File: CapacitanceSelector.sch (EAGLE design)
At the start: 12 parts

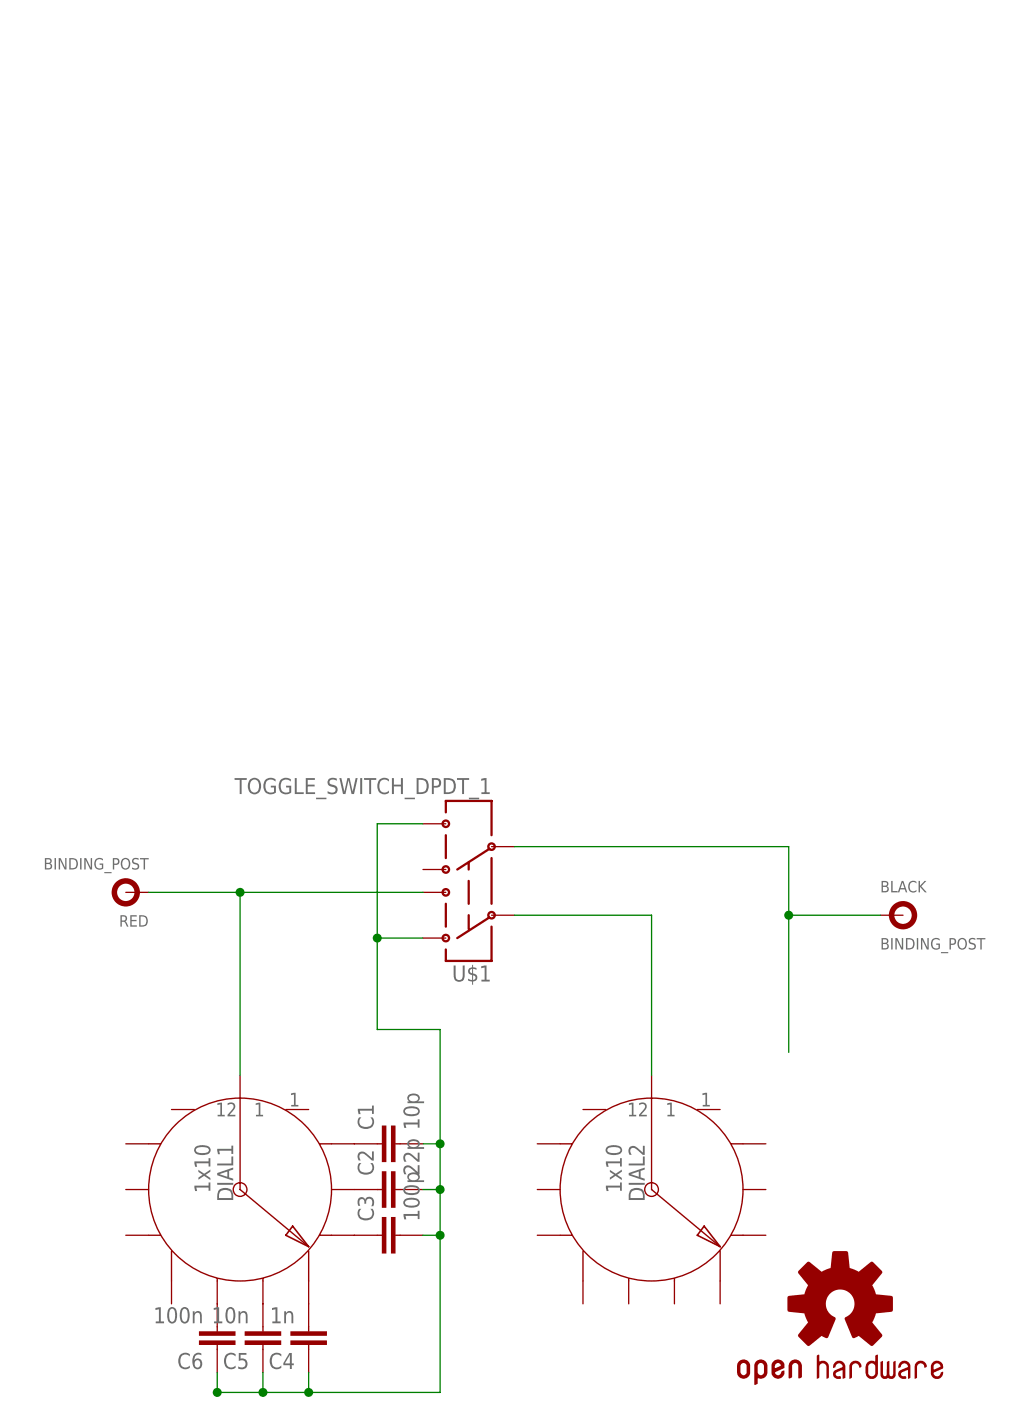
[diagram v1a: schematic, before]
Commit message: This is going to be an overly expensive board
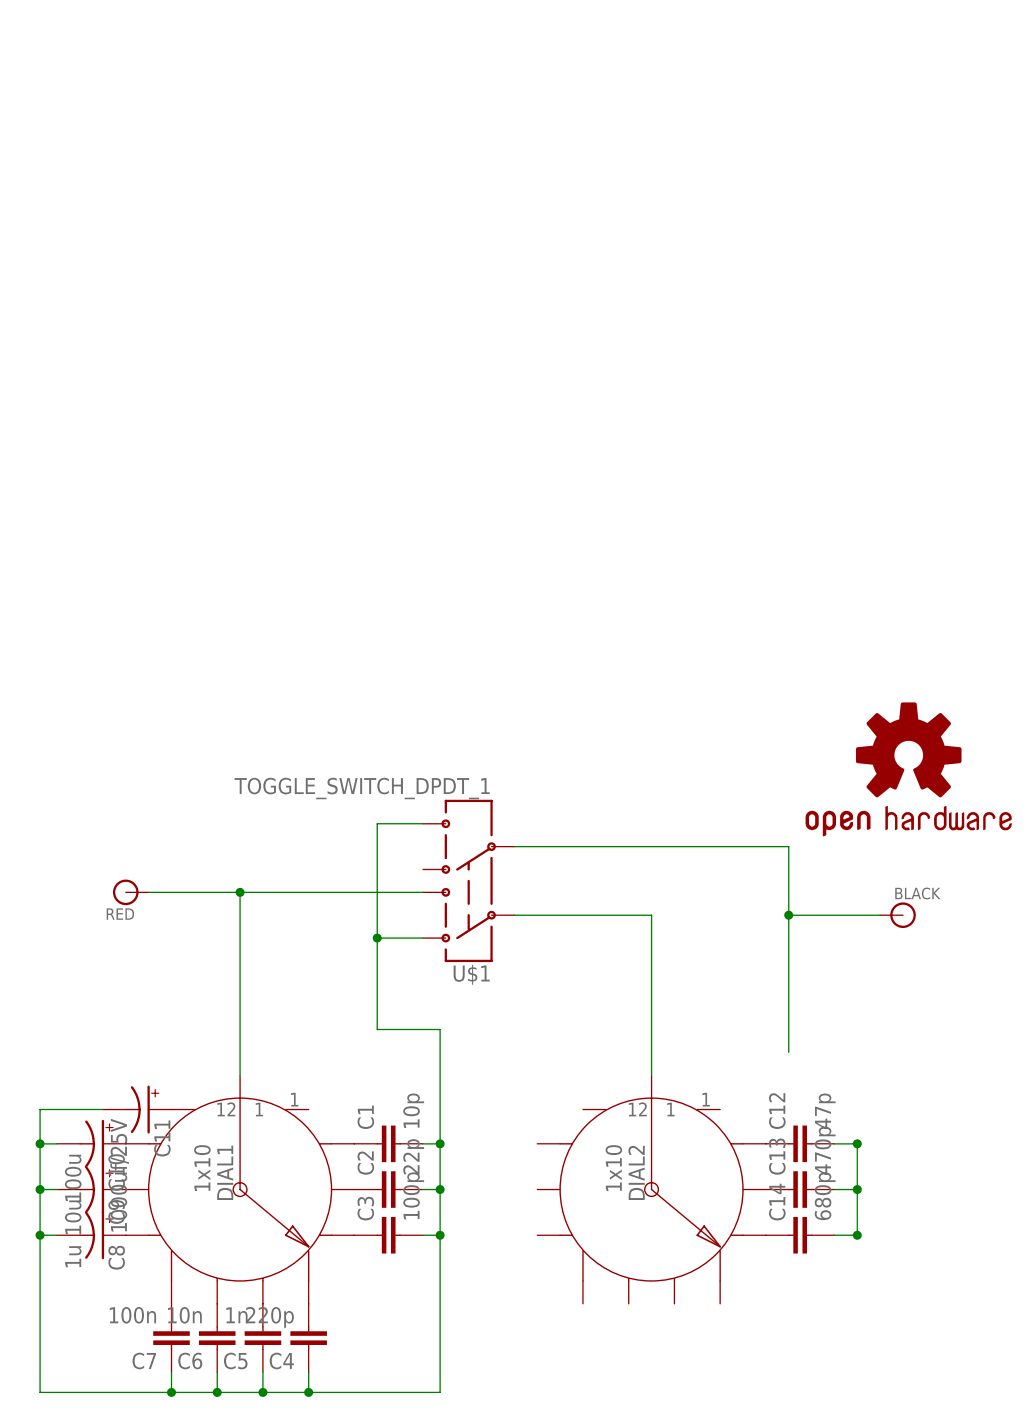
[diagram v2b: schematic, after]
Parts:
- added C10: 100u, SparkFun-Capacitors:10UF-25V-20%(PTH)KIT
- added C11: 1000uf/25V, SparkFun-Capacitors:1000UF-25V(PTH)KIT
- added C12: 47p, SparkFun-Capacitors:CAP_
- added C13: 470p, SparkFun-Capacitors:0.1UF-50V-20%(PTH)KIT-EZ
- added C14: 680p, SparkFun-Capacitors:0.1UF-50V-20%(PTH)KIT-EZ
- added C7: 100n, SparkFun-Capacitors:0.1UF-50V-20%(PTH)KIT-EZ
- added C8: 1u, SparkFun-Capacitors:10UF-25V-20%(PTH)KIT
- added C9: 10u, SparkFun-Capacitors:10UF-25V-20%(PTH)KIT
- BLACK, RED: value BINDING_POST -> (none); device SparkFun-Connectors:BINDING_POST -> SparkFun-Connectors:BANANA_CONN
- C4: value 1n -> 220p
- C5: value 10n -> 1n
- C6: value 100n -> 10n
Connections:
- new net N$11: C13.1, DIAL2.3
- new net N$13: C8.+, DIAL1.9
- new net N$14: C12.2, C13.2, C14.2
- new net N$15: C14.1, DIAL2.4
- new net N$16: C11.+, DIAL1.12
- new net N$17: C7.2, DIAL1.8
- new net N$2: C12.1, DIAL2.2
- new net N$20: C10.+, DIAL1.11
- new net N$21: C9.+, DIAL1.10
- net N$1: now also RED.1; no longer RED.P$1
- net N$12: now also C10.-, C11.-, C7.1, C8.-, C9.-
- net N$3: now also BLACK.1; no longer BLACK.P$1
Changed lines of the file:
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@@
 <setting verticaltext="up"/>
 </settings>
-<grid distance="0.0125" unitdist="inch" unit="mm" style="lines" multiple="1" display="no" altdistance="0.00125" altunitdist="inch" altunit="mm"/>
+<grid distance="0.0125" unitdist="inch" unit="inch" style="lines" multiple="1" display="no" altdistance="0.00125" altunitdist="inch" altunit="inch"/>
 <layers>
 <layer number="1" name="Top" color="4" fill="1" visible="no" active="no"/>
@@
 <part name="DIAL1" library="HokieGeek" deviceset="SWITCH_ROTARY_1X12" device="" value="1x10"/>
 <part name="DIAL2" library="HokieGeek" deviceset="SWITCH_ROTARY_1X12" device="" value="1x10"/>
-<part name="RED" library="SparkFun-Connectors" deviceset="BINDING_POST" device=""/>
-<part name="BLACK" library="SparkFun-Connectors" deviceset="BINDING_POST" device=""/>
 <part name="LOGO1" library="SparkFun-Aesthetics" deviceset="OSHW-LOGO" device="L"/>
 <part name="U$1" library="HokieGeek" deviceset="TOGGLE_SWITCH_DPDT_1" device=""/>
@@
 <part name="C2" library="SparkFun-Capacitors" deviceset="0.1UF-50V-20%(PTH)" device="KIT-EZ" value="22p"/>
 <part name="C3" library="SparkFun-Capacitors" deviceset="0.1UF-50V-20%(PTH)" device="KIT-EZ" value="100p"/>
-<part name="C4" library="SparkFun-Capacitors" deviceset="0.1UF-50V-20%(PTH)" device="KIT-EZ" value="1n"/>
-<part name="C5" library="SparkFun-Capacitors" deviceset="0.1UF-50V-20%(PTH)" device="KIT-EZ" value="10n"/>
-<part name="C6" library="SparkFun-Capacitors" deviceset="0.1UF-50V-20%(PTH)" device="KIT-EZ" value="100n"/>
+<part name="C4" library="SparkFun-Capacitors" deviceset="0.1UF-50V-20%(PTH)" device="KIT-EZ" value="220p"/>
+<part name="C5" library="SparkFun-Capacitors" deviceset="0.1UF-50V-20%(PTH)" device="KIT-EZ" value="1n"/>
+<part name="C6" library="SparkFun-Capacitors" deviceset="0.1UF-50V-20%(PTH)" device="KIT-EZ" value="10n"/>
+<part name="C13" library="SparkFun-Capacitors" deviceset="0.1UF-50V-20%(PTH)" device="KIT-EZ" value="470p"/>
+<part name="C12" library="SparkFun-Capacitors" deviceset="CAP" device="_" value="47p"/>
+<part name="C14" library="SparkFun-Capacitors" deviceset="0.1UF-50V-20%(PTH)" device="KIT-EZ" value="680p"/>
+<part name="C11" library="SparkFun-Capacitors" deviceset="1000UF-25V(PTH)" device="KIT" value="1000uf/25V"/>
+<part name="C9" library="SparkFun-Capacitors" deviceset="10UF-25V-20%(PTH)" device="KIT" value="10u"/>
+<part name="C10" library="SparkFun-Capacitors" deviceset="10UF-25V-20%(PTH)" device="KIT" value="100u"/>
+<part name="C7" library="SparkFun-Capacitors" deviceset="0.1UF-50V-20%(PTH)" device="KIT-EZ" value="100n"/>
+<part name="C8" library="SparkFun-Capacitors" deviceset="10UF-25V-20%(PTH)" device="KIT" value="1u"/>
+<part name="RED" library="SparkFun-Connectors" deviceset="BANANA_CONN" device=""/>
+<part name="BLACK" library="SparkFun-Connectors" deviceset="BANANA_CONN" device=""/>
 </parts>
 <sheets>
@@
 <instance part="DIAL1" gate="G$1" x="27.94" y="22.86" rot="R270"/>
 <instance part="DIAL2" gate="G$1" x="73.66" y="22.86" rot="R270"/>
-<instance part="RED" gate="G$1" x="15.24" y="55.88" rot="R180"/>
-<instance part="BLACK" gate="G$1" x="101.6" y="53.34"/>
-<instance part="LOGO1" gate="G$1" x="94.615" y="10.16"/>
+<instance part="LOGO1" gate="G$1" x="102.235" y="71.12"/>
 <instance part="U$1" gate="G$1" x="53.34" y="55.88" rot="R180"/>
 <instance part="C1" gate="G$1" x="45.72" y="27.94" rot="R90"/>
@@
 <instance part="C5" gate="G$1" x="30.48" y="7.62" rot="R180"/>
 <instance part="C6" gate="G$1" x="25.4" y="7.62" rot="R180"/>
+<instance part="C13" gate="G$1" x="91.44" y="22.86" rot="R90"/>
+<instance part="C12" gate="G$1" x="91.44" y="27.94" rot="R90"/>
+<instance part="C14" gate="G$1" x="91.44" y="17.78" rot="R90"/>
+<instance part="C11" gate="G$1" x="17.78" y="31.75" rot="R270"/>
+<instance part="C9" gate="G$1" x="12.7" y="22.86" rot="R270"/>
+<instance part="C10" gate="G$1" x="12.7" y="27.94" rot="R270"/>
+<instance part="C7" gate="G$1" x="20.32" y="7.62" rot="R180"/>
+<instance part="C8" gate="G$1" x="12.7" y="17.78" rot="R270"/>
+<instance part="RED" gate="G$1" x="15.24" y="55.88" rot="R180"/>
+<instance part="BLACK" gate="G$1" x="101.6" y="53.34"/>
 </instances>
 <busses>
@@
 <pinref part="DIAL1" gate="G$1" pin="COMMON"/>
 <wire x1="27.94" y1="35.56" x2="27.94" y2="55.88" width="0.1524" layer="91"/>
-<pinref part="RED" gate="G$1" pin="P$1"/>
 <wire x1="27.94" y1="55.88" x2="17.78" y2="55.88" width="0.1524" layer="91"/>
 <wire x1="48.26" y1="55.88" x2="27.94" y2="55.88" width="0.1524" layer="91"/>
 <junction x="27.94" y="55.88"/>
 <pinref part="U$1" gate="G$1" pin="3"/>
+<pinref part="RED" gate="G$1" pin="1"/>
 </segment>
 </net>
 <net name="N$3" class="0">
 <segment>
-<pinref part="BLACK" gate="G$1" pin="P$1"/>
 <wire x1="99.06" y1="53.34" x2="88.9" y2="53.34" width="0.1524" layer="91"/>
 <wire x1="88.9" y1="53.34" x2="88.9" y2="38.1" width="0.1524" layer="91"/>
@@
 <wire x1="88.9" y1="60.96" x2="88.9" y2="53.34" width="0.1524" layer="91"/>
 <pinref part="U$1" gate="G$1" pin="5"/>
+<pinref part="BLACK" gate="G$1" pin="1"/>
 </segment>
 </net>
@@
 <wire x1="50.165" y1="27.94" x2="50.165" y2="40.64" width="0.1524" layer="91"/>
 <wire x1="50.165" y1="40.64" x2="43.18" y2="40.64" width="0.1524" layer="91"/>
-<junction x="25.4" y="0.3175"/>
 <junction x="50.165" y="27.94"/>
 <junction x="50.165" y="22.86"/>
@@
 <wire x1="35.56" y1="2.54" x2="35.56" y2="0.3175" width="0.1524" layer="91"/>
 <junction x="35.56" y="0.3175"/>
-</segment>
-</net>
+<wire x1="25.4" y1="0.3175" x2="20.32" y2="0.3175" width="0.1524" layer="91"/>
+<wire x1="20.32" y1="0.3175" x2="20.32" y2="2.54" width="0.1524" layer="91"/>
+<pinref part="C7" gate="G$1" pin="1"/>
+<pinref part="C11" gate="G$1" pin="-"/>
+<wire x1="12.7" y1="31.75" x2="5.715" y2="31.75" width="0.1524" layer="91"/>
+<pinref part="C9" gate="G$1" pin="-"/>
+<wire x1="7.62" y1="22.86" x2="5.715" y2="22.86" width="0.1524" layer="91"/>
+<wire x1="5.715" y1="22.86" x2="5.715" y2="27.94" width="0.1524" layer="91"/>
+<pinref part="C10" gate="G$1" pin="-"/>
+<wire x1="5.715" y1="27.94" x2="7.62" y2="27.94" width="0.1524" layer="91"/>
+<wire x1="5.715" y1="31.75" x2="5.715" y2="27.94" width="0.1524" layer="91"/>
+<junction x="5.715" y="22.86"/>
+<junction x="5.715" y="27.94"/>
+<wire x1="20.32" y1="0.3175" x2="5.715" y2="0.3175" width="0.1524" layer="91"/>
+<wire x1="5.715" y1="0.3175" x2="5.715" y2="17.78" width="0.1524" layer="91"/>
+<junction x="20.32" y="0.3175"/>
+<junction x="25.4" y="0.3175"/>
+<pinref part="C8" gate="G$1" pin="-"/>
+<wire x1="5.715" y1="17.78" x2="5.715" y2="22.86" width="0.1524" layer="91"/>
+<wire x1="7.62" y1="17.78" x2="5.715" y2="17.78" width="0.1524" layer="91"/>
+<junction x="5.715" y="17.78"/>
+</segment>
+</net>
+<net name="N$11" class="0">
+<segment>
+<pinref part="DIAL2" gate="G$1" pin="3"/>
+<pinref part="C13" gate="G$1" pin="1"/>
+</segment>
+</net>
+<net name="N$2" class="0">
+<segment>
+<pinref part="DIAL2" gate="G$1" pin="2"/>
+<pinref part="C12" gate="G$1" pin="1"/>
+</segment>
+</net>
+<net name="N$14" class="0">
+<segment>
+<pinref part="C12" gate="G$1" pin="2"/>
+<wire x1="93.98" y1="27.94" x2="96.52" y2="27.94" width="0.1524" layer="91"/>
+<wire x1="96.52" y1="27.94" x2="96.52" y2="22.86" width="0.1524" layer="91"/>
+<pinref part="C13" gate="G$1" pin="2"/>
+<wire x1="96.52" y1="22.86" x2="93.98" y2="22.86" width="0.1524" layer="91"/>
+<junction x="96.52" y="22.86"/>
+<junction x="96.52" y="27.94"/>
+<pinref part="C14" gate="G$1" pin="2"/>
+<wire x1="93.98" y1="17.78" x2="96.52" y2="17.78" width="0.1524" layer="91"/>
+<wire x1="96.52" y1="17.78" x2="96.52" y2="22.86" width="0.1524" layer="91"/>
+<junction x="96.52" y="17.78"/>
+</segment>
+</net>
+<net name="N$15" class="0">
+<segment>
+<pinref part="DIAL2" gate="G$1" pin="4"/>
+<pinref part="C14" gate="G$1" pin="1"/>
+</segment>
+</net>
+<net name="N$16" class="0">
+<segment>
+<pinref part="DIAL1" gate="G$1" pin="12"/>
+<pinref part="C11" gate="G$1" pin="+"/>
+</segment>
+</net>
+<net name="N$17" class="0">
+<segment>
+<pinref part="DIAL1" gate="G$1" pin="8"/>
+<pinref part="C7" gate="G$1" pin="2"/>
+</segment>
+</net>
+<net name="N$20" class="0">
+<segment>
+<pinref part="DIAL1" gate="G$1" pin="11"/>
+<pinref part="C10" gate="G$1" pin="+"/>
+</segment>
+</net>
+<net name="N$21" class="0">
+<segment>
+<pinref part="DIAL1" gate="G$1" pin="10"/>
+<pinref part="C9" gate="G$1" pin="+"/>
+</segment>
+</net>
+<net name="N$13" class="0">
+<segment>
+<pinref part="DIAL1" gate="G$1" pin="9"/>
+<pinref part="C8" gate="G$1" pin="+"/>
+</segment>
+</net>
